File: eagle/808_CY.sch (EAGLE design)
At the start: 130 parts, among them Q1 2N3904, Q2 2N3904, Q3 2N3904, Q4 2N3904, Q5 2N3904, Q6 2N3904, Q7 2N3904, Q8 2N3906, U1 4584N, U3 µPC4558C, U5 µPC4558C, U6 µPC4558C

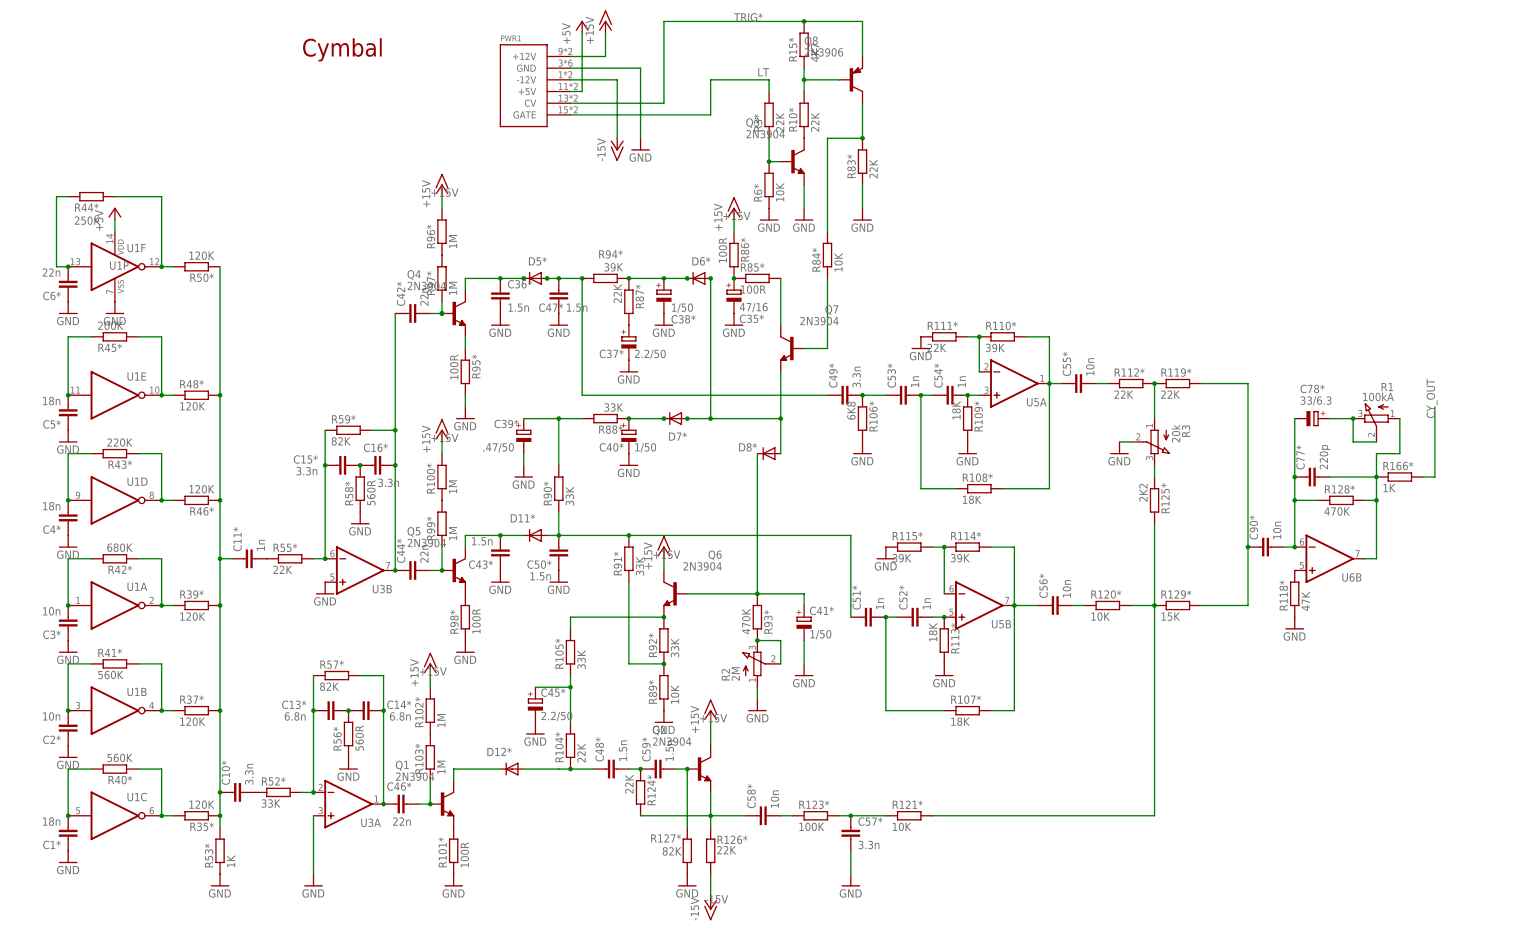
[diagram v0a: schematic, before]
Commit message: subbed opamps
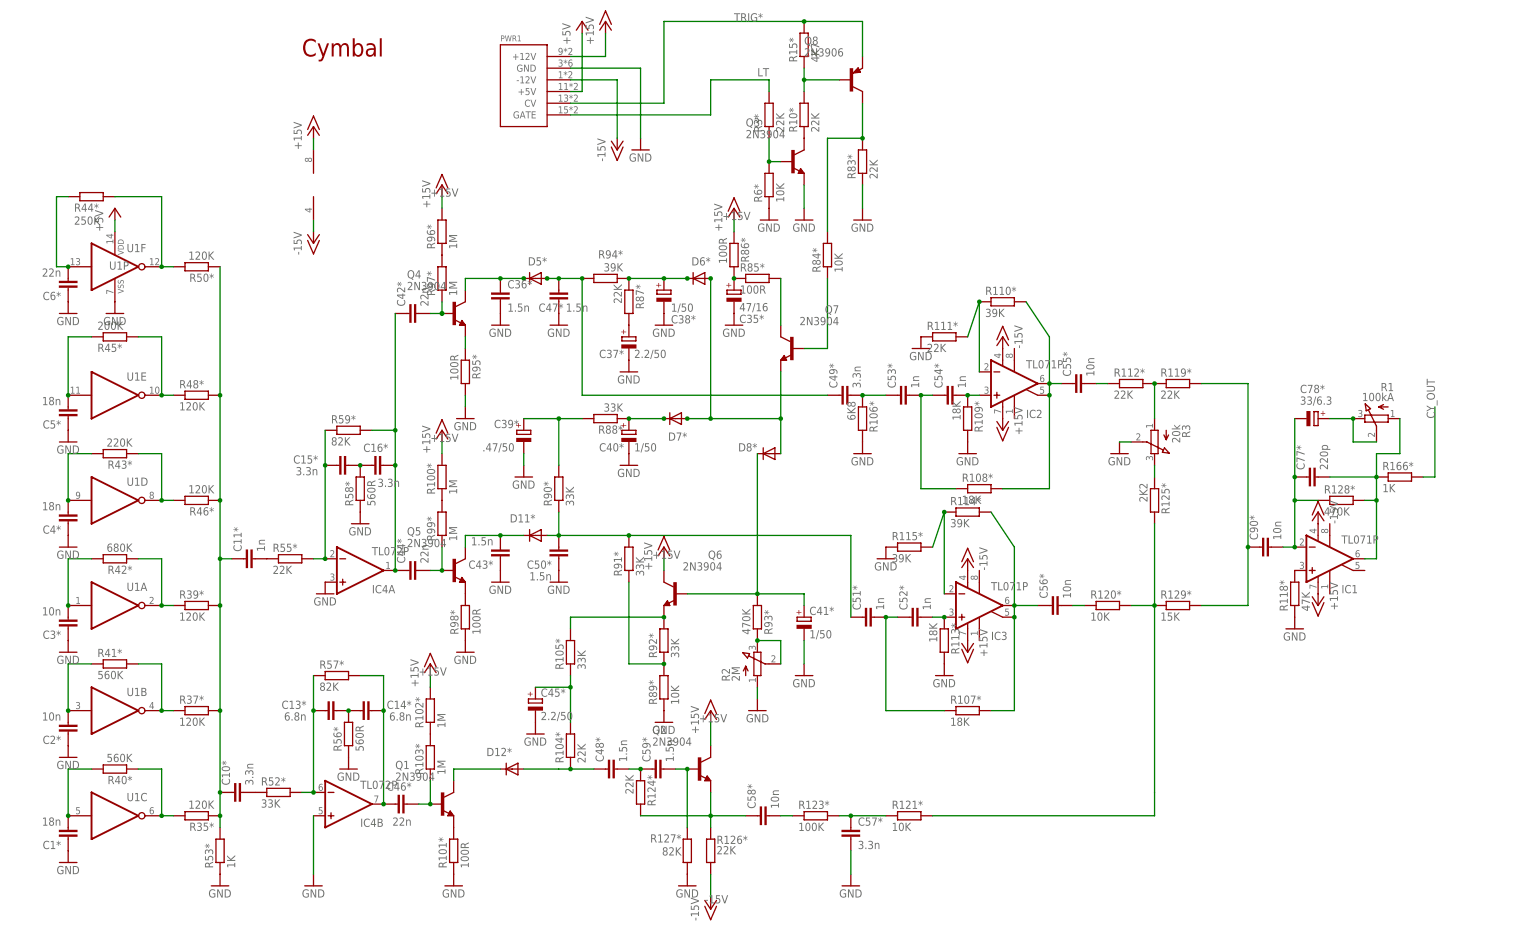
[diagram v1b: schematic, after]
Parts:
- removed U3, U5, U6: µPC4558C, TR808clone:µPC4558C
- added IC1, IC2, IC3: TL071P, linear:TL071P
- added IC4: TL072P, linear:TL072P
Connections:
- removed net N$182: R118*.2, U6B.+IN
- new net N$4: IC1.+IN, R118*.2
- net +15V: now also IC1.V+, IC2.V+, IC3.V+, IC4P.V+
- net -15V: now also IC1.V-, IC2.V-, IC3.V-, IC4P.V-
- net GND: now also IC4A.+IN, IC4B.+IN; no longer U3A.+IN, U3B.+IN
- net N$496: now also IC4A.-IN; no longer U3B.-IN
- net N$503: now also IC4B.-IN; no longer U3A.-IN
- net N$504: now also IC4B.OUT; no longer U3A.OUT
- net N$531: now also IC2.+IN; no longer U5A.+IN
- net N$533: now also IC2.ON2, IC2.OUT; no longer U5A.OUT
- net N$535: now also IC2.-IN; no longer U5A.-IN
- net N$538: now also IC3.+IN; no longer U5B.+IN
- net N$539: now also IC3.ON2, IC3.OUT; no longer U5B.OUT
- net N$541: now also IC3.-IN; no longer U5B.-IN
- net N$544: now also IC1.-IN; no longer U6B.-IN
- net N$546: now also IC1.OUT; no longer U6B.OUT
- net TO_HH: now also IC4A.OUT; no longer U3B.OUT
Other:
- moved on the sheet: R110*, R114*

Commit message: moved diginoise off-board
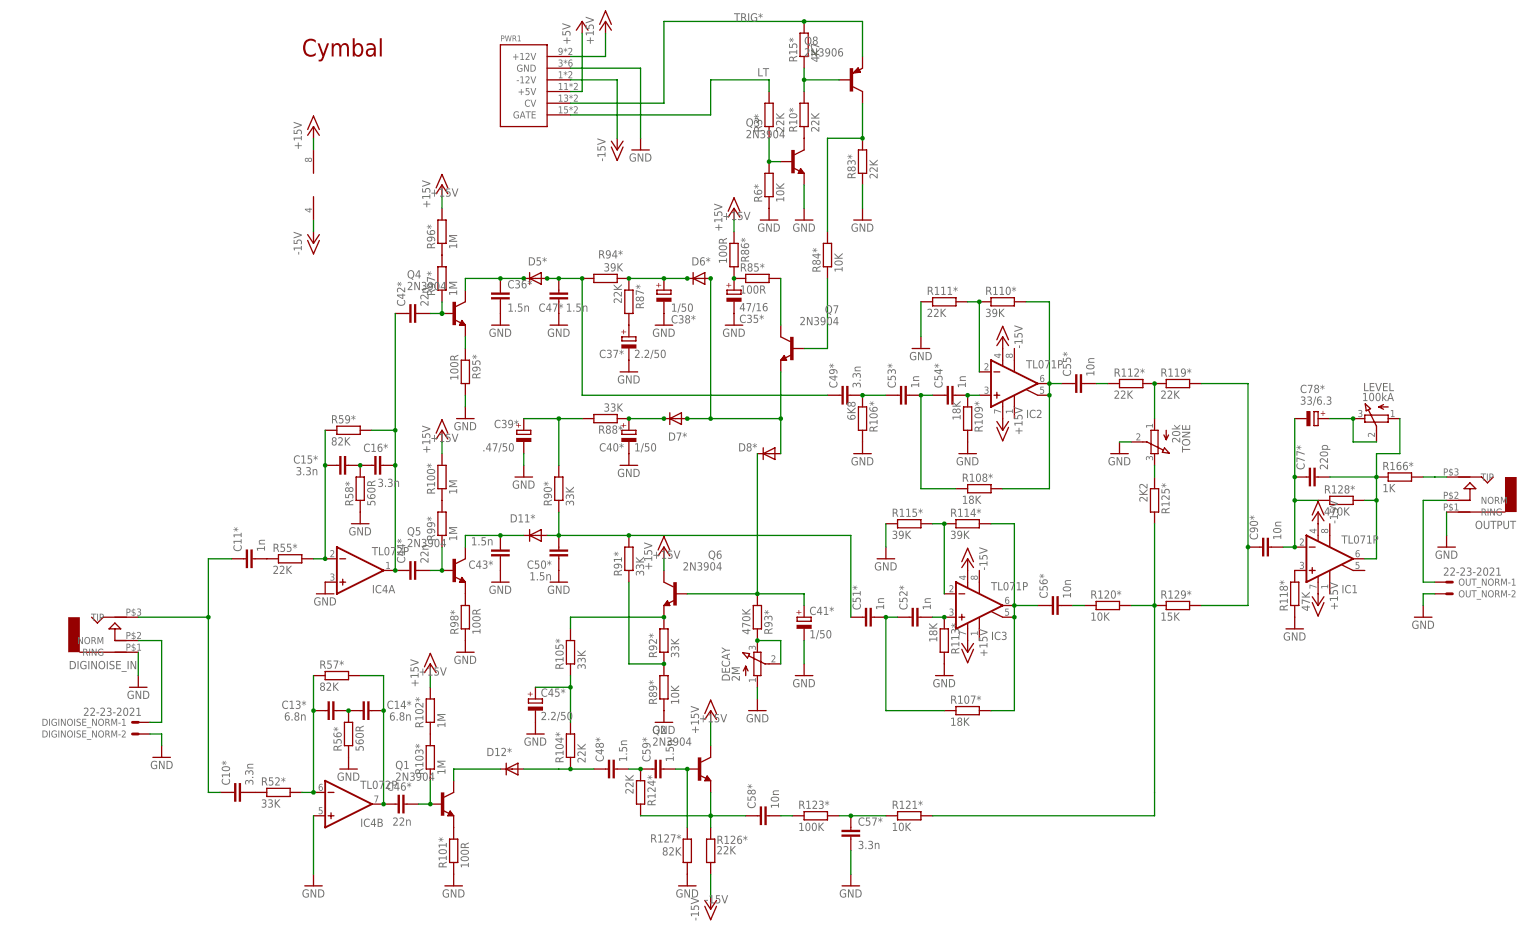
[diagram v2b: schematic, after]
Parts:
- removed C1*, C4*, C5*: 18n, TR808clone:C-EU4MM_PITCH
- removed C2*, C3*: 10n, TR808clone:C-EU3.5MM_PITCH
- removed C6*: 22n, TR808clone:C-EU4MM_PITCH
- removed R35*, R37*, R39*, R46*, R48*, R50*: 120K, TR808clone:R-EU_0207/5V
- removed R40*, R41*: 560K, TR808clone:R-EU_0207/5V
- removed R42*: 680K, TR808clone:R-EU_0207/5V
- removed R43*: 220K, TR808clone:R-EU_0207/5V
- removed R44*: 250K, TR808clone:R-EU_0207/5V
- removed R45*: 200K, TR808clone:R-EU_0207/5V
- removed R53*: 1K, TR808clone:R-EU_0207/5V
- removed U1: 4584N, TR808clone:4584N
- added DIGINOISE_IN, OUTPUT: AUDIO-JACK, erthenvar:AUDIO-JACK
- added DIGINOISE_NORM, OUT_NORM: 22-23-2021, con-molex:22-23-2021
- renumbered R1 to LEVEL, R2 to DECAY, R3 to TONE
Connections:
- removed net N$183: C1*.2, R40*.2, U1C.I
- removed net N$184: C2*.2, R41*.1, U1B.I
- removed net N$185: C3*.2, R42*.2, U1A.I
- removed net N$186: C4*.2, R43*.2, U1D.I
- removed net N$194: R35*.2, R40*.1, U1C.O
- removed net N$201: R37*.1, R41*.2, U1B.O
- removed net N$210: R43*.1, R46*.2, U1D.O
- removed net N$213: C5*.2, R45*.1, U1E.I
- removed net N$214: C6*.2, R44*.1, U1F.I
- removed net N$215: R39*.1, R42*.1, U1A.O
- removed net N$485: C10*.1, C11*.1, R35*.1, R37*.2, R39*.2, R46*.1, R48*.2, R50*.1, R53*.2
- removed net TP6: R44*.2, R50*.2, U1F.O
- removed net TP7: R45*.2, R48*.1, U1E.O
- new net LT_LC_OUT: OUTPUT.TIP
- new net LT_LC_OUT1: C10*.1, C11*.1, DIGINOISE_IN.TIP
- new net N$5: OUTPUT.NORM, OUT_NORM-1.S
- new net N$6: DIGINOISE_IN.NORM, DIGINOISE_NORM-1.S
- net +5V: no longer U1P.VDD
- net GND: now also DIGINOISE_IN.RING, DIGINOISE_NORM-2.S, OUTPUT.RING, OUT_NORM-2.S; no longer C1*.1, C2*.1, C3*.1, C4*.1, C5*.1, C6*.1, R53*.1, U1P.VSS
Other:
- moved on the sheet: R111*, R114*, R115*

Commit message: corrected bad connection on 071s
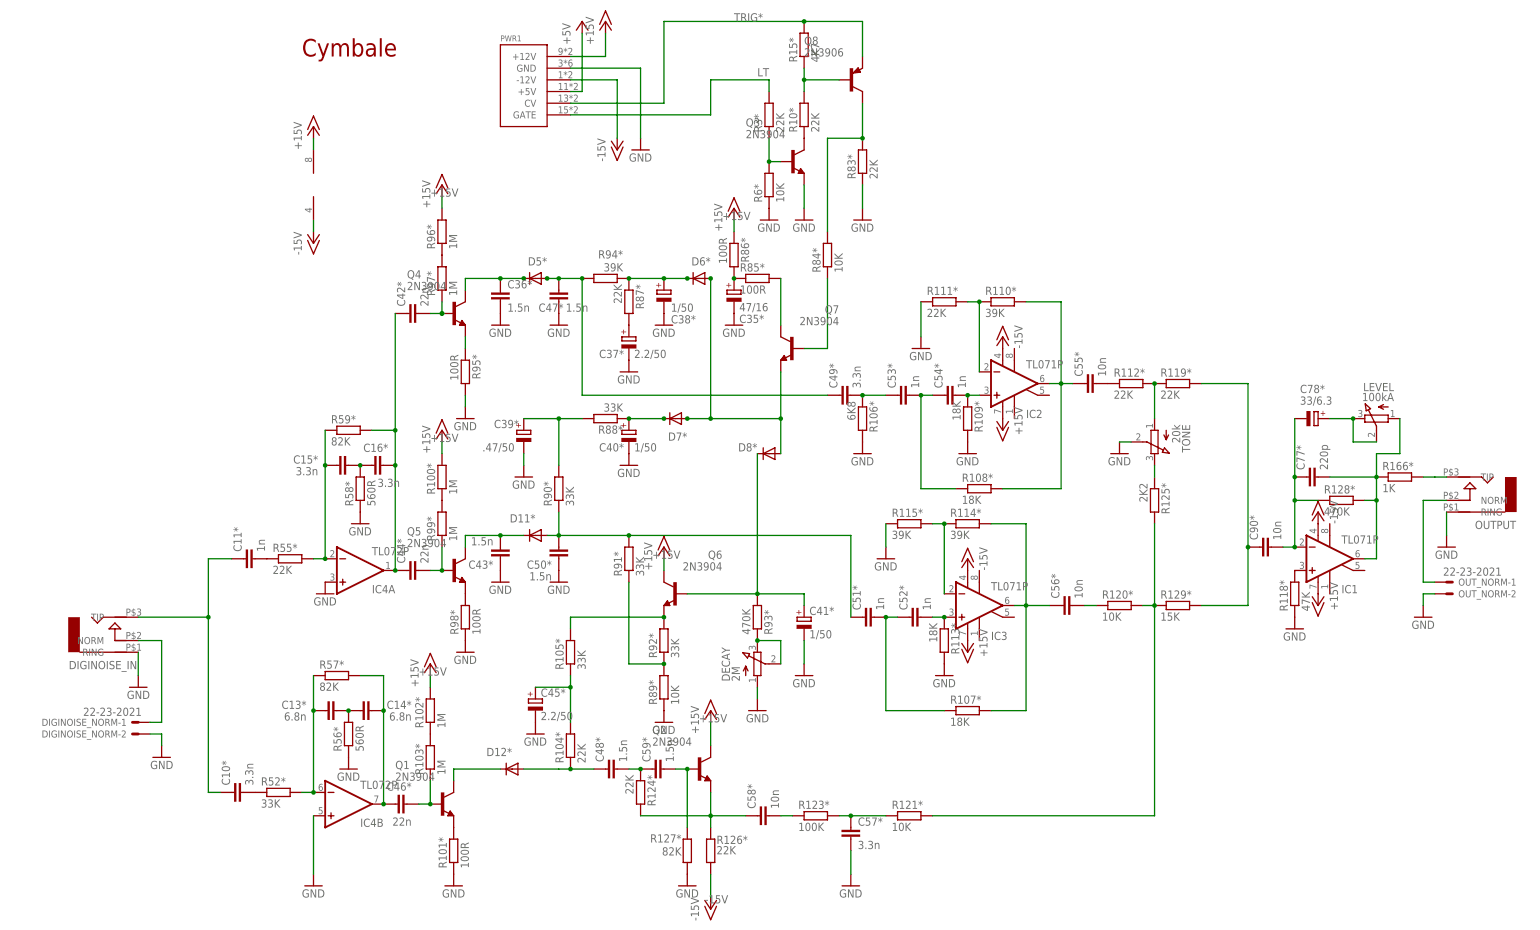
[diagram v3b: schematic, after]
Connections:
- net N$533: no longer IC2.ON2
- net N$539: no longer IC3.ON2
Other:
- note added: "Cymbale"
- note removed: "Cymbal"
- moved on the sheet: C55*, C56*, R120*
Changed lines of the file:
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@@
 <sheet>
 <plain>
-<text x="-33.02" y="149.86" size="3.81" layer="94">Cymbal</text>
+<text x="-33.02" y="149.86" size="3.81" layer="94">Cymbale</text>
 </plain>
 <instances>
@@
 <instance part="V341" gate="1" x="101.6" y="86.36"/>
 <instance part="R110*" gate="G$1" x="119.38" y="96.52"/>
-<instance part="C55*" gate="G$1" x="134.62" y="78.74" rot="R90"/>
+<instance part="C55*" gate="G$1" x="137.16" y="78.74" rot="R90"/>
 <instance part="R112*" gate="G$1" x="147.32" y="78.74"/>
 <instance part="R119*" gate="G$1" x="157.48" y="78.74"/>
@@
 <instance part="V344" gate="1" x="106.68" y="15.24"/>
 <instance part="C51*" gate="G$1" x="88.9" y="27.94" rot="R90"/>
-<instance part="C56*" gate="G$1" x="129.54" y="30.48" rot="R90"/>
-<instance part="R120*" gate="G$1" x="142.24" y="30.48"/>
+<instance part="C56*" gate="G$1" x="132.08" y="30.48" rot="R90"/>
+<instance part="R120*" gate="G$1" x="144.78" y="30.48"/>
 <instance part="R129*" gate="G$1" x="157.48" y="30.48"/>
 <instance part="R128*" gate="G$1" x="193.04" y="53.34"/>
@@
 <net name="N$533" class="0">
 <segment>
-<wire x1="124.46" y1="96.52" x2="129.54" y2="96.52" width="0.1524" layer="91"/>
-<wire x1="129.54" y1="96.52" x2="129.54" y2="78.74" width="0.1524" layer="91"/>
+<pinref part="R108*" gate="G$1" pin="2"/>
+<wire x1="119.38" y1="55.88" x2="132.08" y2="55.88" width="0.1524" layer="91"/>
+<pinref part="R110*" gate="G$1" pin="2"/>
+<wire x1="124.46" y1="96.52" x2="132.08" y2="96.52" width="0.1524" layer="91"/>
+<pinref part="C55*" gate="G$1" pin="1"/>
 <wire x1="129.54" y1="78.74" x2="132.08" y2="78.74" width="0.1524" layer="91"/>
-<pinref part="C55*" gate="G$1" pin="1"/>
-<pinref part="R110*" gate="G$1" pin="2"/>
-<junction x="129.54" y="78.74"/>
-<pinref part="R108*" gate="G$1" pin="2"/>
-<wire x1="119.38" y1="55.88" x2="129.54" y2="55.88" width="0.1524" layer="91"/>
-<wire x1="129.54" y1="55.88" x2="129.54" y2="76.2" width="0.1524" layer="91"/>
-<pinref part="IC2" gate="A" pin="ON2"/>
-<wire x1="129.54" y1="76.2" x2="129.54" y2="78.74" width="0.1524" layer="91"/>
-<junction x="129.54" y="76.2"/>
 <pinref part="IC2" gate="A" pin="OUT"/>
+<wire x1="132.08" y1="78.74" x2="134.62" y2="78.74" width="0.1524" layer="91"/>
+<wire x1="132.08" y1="96.52" x2="132.08" y2="78.74" width="0.1524" layer="91"/>
+<junction x="132.08" y="78.74"/>
+<wire x1="132.08" y1="55.88" x2="132.08" y2="78.74" width="0.1524" layer="91"/>
 </segment>
 </net>
@@
 <net name="N$536" class="0">
 <segment>
-<wire x1="139.7" y1="78.74" x2="142.24" y2="78.74" width="0.1524" layer="91"/>
 <pinref part="C55*" gate="G$1" pin="2"/>
 <pinref part="R112*" gate="G$1" pin="1"/>
@@
 <net name="N$539" class="0">
 <segment>
-<wire x1="116.84" y1="48.26" x2="121.92" y2="48.26" width="0.1524" layer="91"/>
-<wire x1="121.92" y1="48.26" x2="121.92" y2="30.48" width="0.1524" layer="91"/>
-<wire x1="121.92" y1="30.48" x2="127" y2="30.48" width="0.1524" layer="91"/>
+<wire x1="116.84" y1="48.26" x2="124.46" y2="48.26" width="0.1524" layer="91"/>
 <pinref part="R114*" gate="G$1" pin="2"/>
+<pinref part="R107*" gate="G$1" pin="2"/>
+<wire x1="116.84" y1="7.62" x2="124.46" y2="7.62" width="0.1524" layer="91"/>
 <pinref part="C56*" gate="G$1" pin="1"/>
-<junction x="121.92" y="30.48"/>
-<pinref part="R107*" gate="G$1" pin="2"/>
-<wire x1="116.84" y1="7.62" x2="121.92" y2="7.62" width="0.1524" layer="91"/>
-<wire x1="121.92" y1="7.62" x2="121.92" y2="27.94" width="0.1524" layer="91"/>
-<pinref part="IC3" gate="A" pin="ON2"/>
-<wire x1="121.92" y1="27.94" x2="121.92" y2="30.48" width="0.1524" layer="91"/>
-<junction x="121.92" y="27.94"/>
+<wire x1="121.92" y1="30.48" x2="124.46" y2="30.48" width="0.1524" layer="91"/>
 <pinref part="IC3" gate="A" pin="OUT"/>
+<wire x1="124.46" y1="30.48" x2="129.54" y2="30.48" width="0.1524" layer="91"/>
+<wire x1="124.46" y1="7.62" x2="124.46" y2="30.48" width="0.1524" layer="91"/>
+<junction x="124.46" y="30.48"/>
+<wire x1="124.46" y1="48.26" x2="124.46" y2="30.48" width="0.1524" layer="91"/>
 </segment>
 </net>
@@
 <net name="N$547" class="0">
 <segment>
-<wire x1="134.62" y1="30.48" x2="137.16" y2="30.48" width="0.1524" layer="91"/>
 <pinref part="C56*" gate="G$1" pin="2"/>
 <pinref part="R120*" gate="G$1" pin="1"/>
+<wire x1="139.7" y1="30.48" x2="137.16" y2="30.48" width="0.1524" layer="91"/>
 </segment>
 </net>
@@
 <segment>
 <wire x1="152.4" y1="48.26" x2="152.4" y2="30.48" width="0.1524" layer="91"/>
-<wire x1="147.32" y1="30.48" x2="152.4" y2="30.48" width="0.1524" layer="91"/>
-<wire x1="152.4" y1="30.48" x2="152.4" y2="-10.16" width="0.1524" layer="91"/>
+<wire x1="149.86" y1="30.48" x2="152.4" y2="30.48" width="0.1524" layer="91"/>
+<wire x1="152.4" y1="30.48" x2="152.4" y2="-15.24" width="0.1524" layer="91"/>
 <junction x="152.4" y="30.48"/>
 <pinref part="R125*" gate="G$1" pin="2"/>
@@
 <pinref part="R121*" gate="G$1" pin="2"/>
 <wire x1="104.14" y1="-15.24" x2="152.4" y2="-15.24" width="0.1524" layer="91"/>
-<wire x1="152.4" y1="-15.24" x2="152.4" y2="-10.16" width="0.1524" layer="91"/>
-</segment>
-</net>
+</segment>
+</net>
